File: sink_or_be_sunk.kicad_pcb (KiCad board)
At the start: 2 copper layers, 86.1 x 79.7 mm, 82 parts, among them J1 Grid_Conn_LED, J10 Grid_Conn, J11 Grid_Conn, J12 Grid_Conn, J13 Grid_Conn, J14 Grid_Conn, J15 Grid_Conn, J16 Grid_Conn, J18 Keypad_Conn, J19 Display_Conn, J2 Grid_Conn, J20 JTAG_Conn, J21 Debug_Conn, J22 Battery_Conn, J23 USB_B_Micro, J3 Grid_Conn, J4 Grid_Conn, J5 Grid_Conn, J6 Grid_Conn, J7 Grid_Conn, J8 Grid_Conn, J9 Grid_Conn, M1 Motor_DC, Q1 IRL530, Q2 Q_PMOS_GDS, Q3 2N3704, Q4 2N3704, SW1 SW_DPST, SW2 Reset_SW, U1 SN74HC151N, U2 SwitchingRegulator, U3 MCP73831-2-OT, U4 MCP608, U5 ESP32-WROOM-32, U6 CY7C65213A-28PVXI

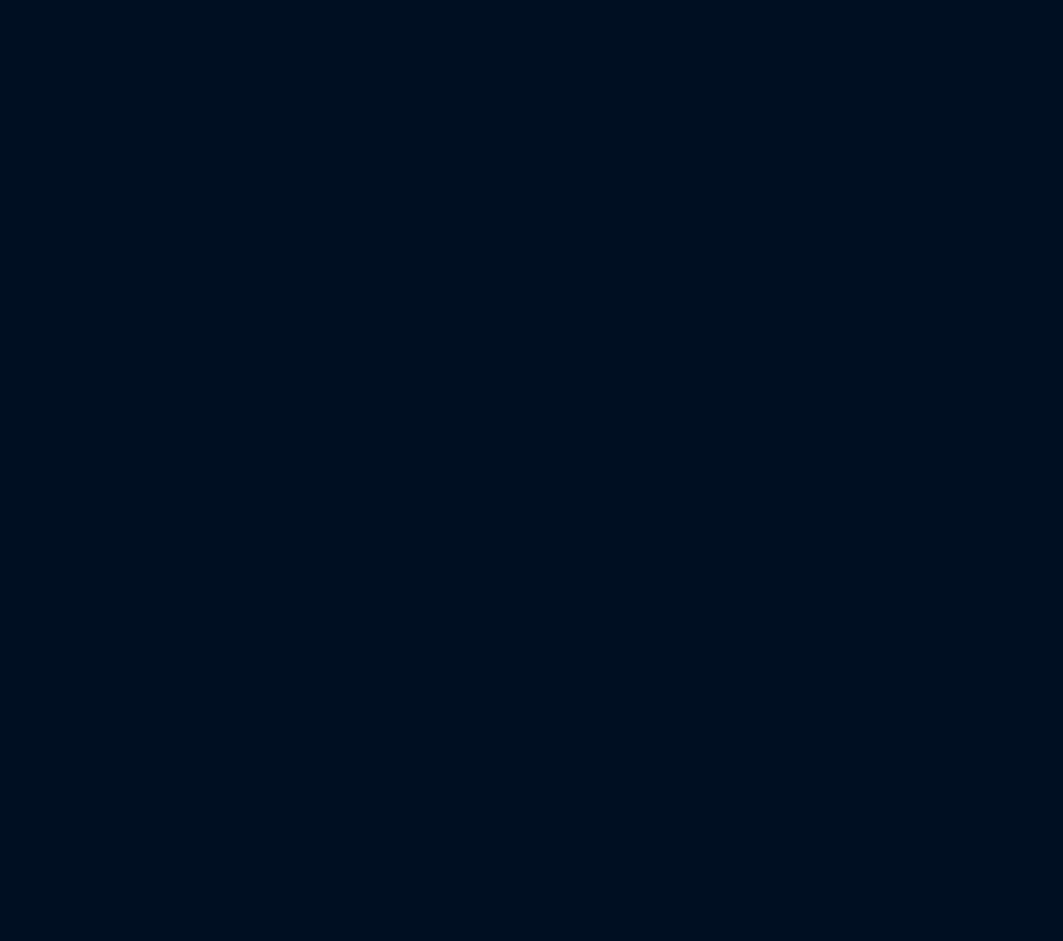
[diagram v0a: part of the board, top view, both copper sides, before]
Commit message: cleaned up footprints
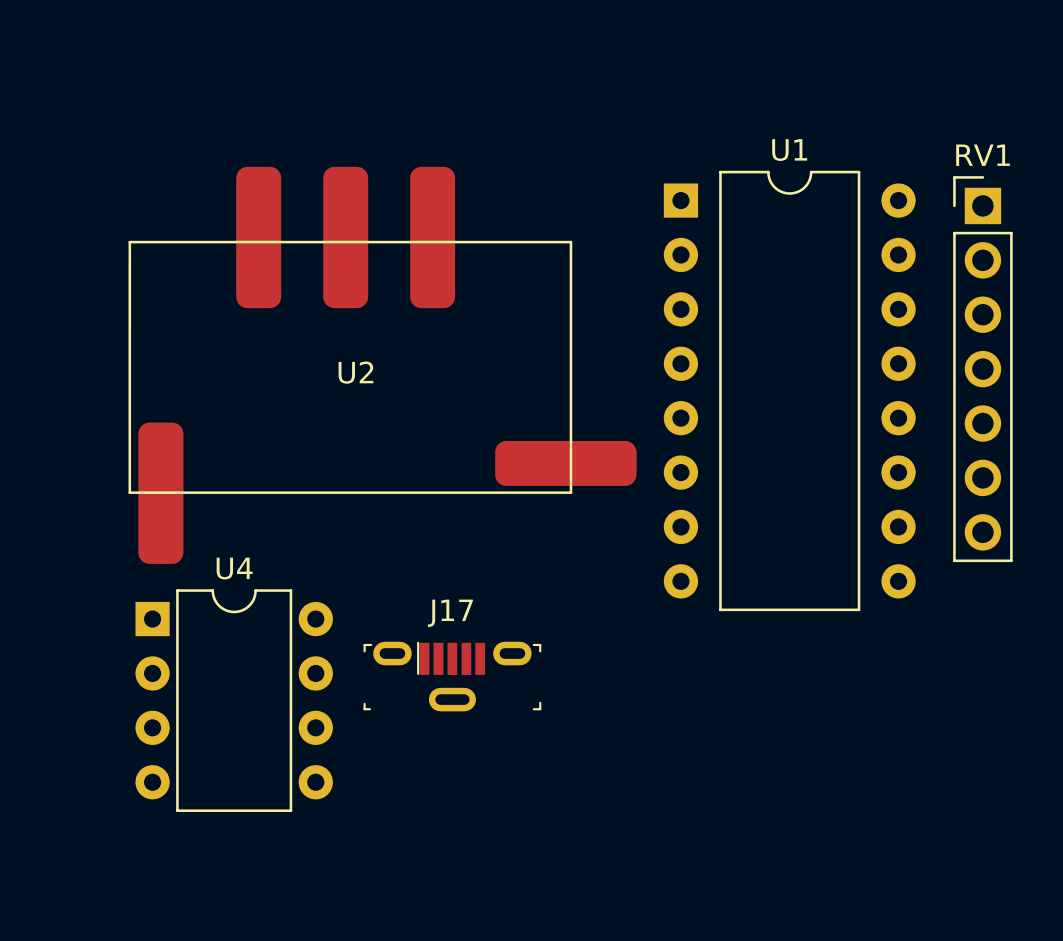
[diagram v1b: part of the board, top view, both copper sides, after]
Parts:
- added J17: USB_B_Micro, PCB_ESP32:USB_Micro_B_Female_Vert_1051330001, F.Cu at (218.7, 112.8)
- added RV1: R_POT, Connector_PinHeader_2.54mm:PinHeader_1x07_P2.54mm_Vertical, F.Cu at (243.5, 91.7)
- added U1: SN74HC151N, Package_DIP:DIP-16_W10.16mm, F.Cu at (229.4, 91.4)
- added U2: SwitchingRegulator, PCB_ESP32:SwitchingRegulator, F.Cu at (214.2, 99.0)
- added U4: MCP608, Package_DIP:DIP-8_W7.62mm, F.Cu at (204.7, 111.0)
- J1: footprint conn:TE_640456-7 -> JST_Conn:TE_640456-7
- J10, J11, J12, J13, J14, J15, J16, J9: footprint conn:TE_640456-2 -> JST_Conn:TE_640456-2
- J2, J3, J4, J5, J6, J7, J8: footprint conn:TE_640456-6 -> JST_Conn:TE_640456-6
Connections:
- U6 pad 15: Net-(J23-Pad3) -> Net-(J17-Pad3)
- U6 pad 16: Net-(J23-Pad2) -> Net-(J17-Pad2)

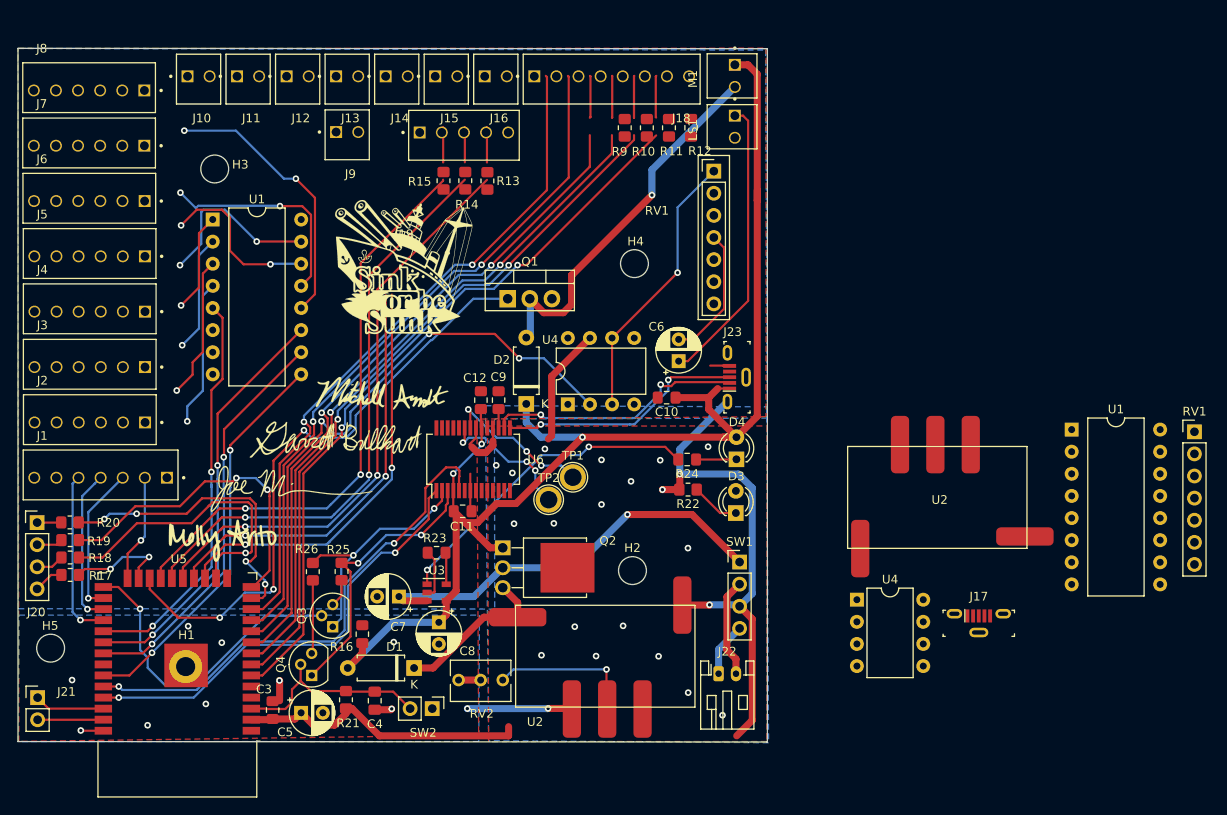
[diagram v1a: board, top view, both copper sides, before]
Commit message: brought over board from regulator
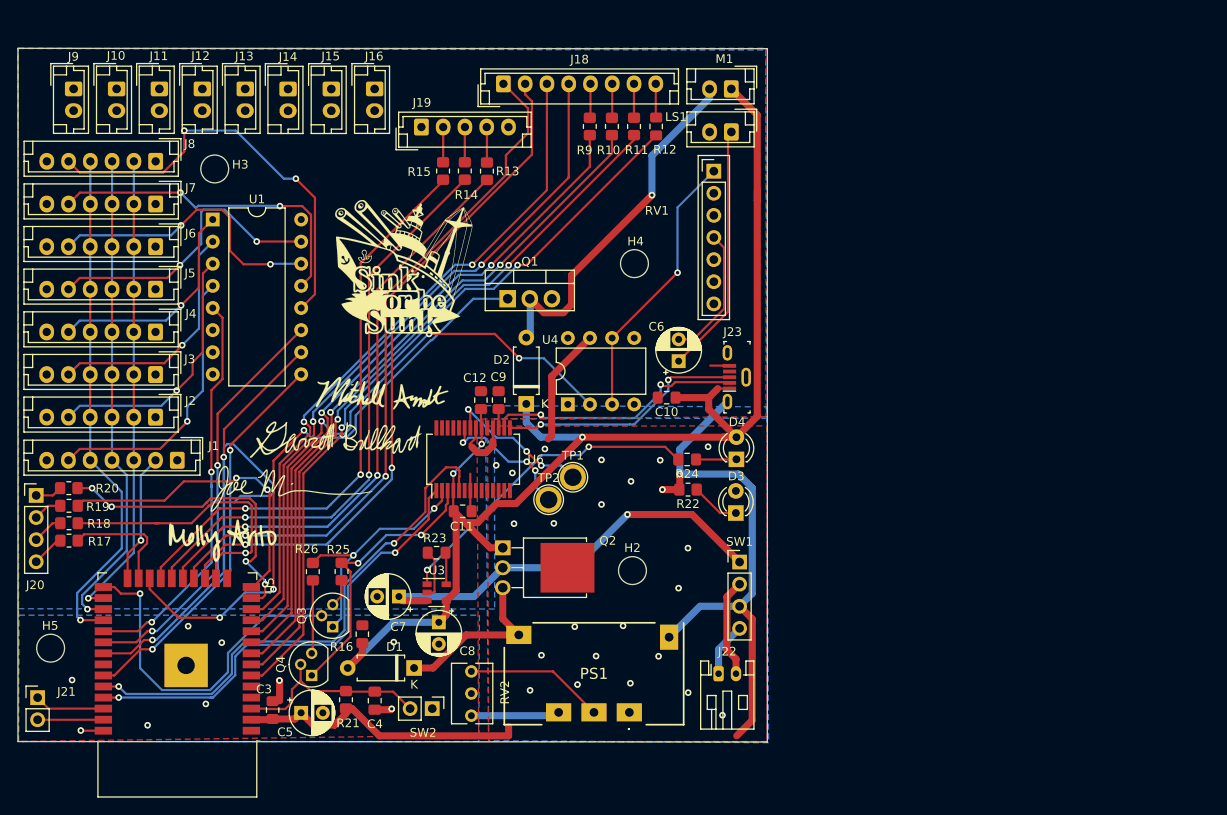
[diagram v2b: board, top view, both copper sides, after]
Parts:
- removed H1: ESP_GND_Pad_Hole, MountingHole:MountingHole_2.2mm_M2_DIN965_Pad
- removed J17: USB_B_Micro, PCB_ESP32:USB_Micro_B_Female_Vert_1051330001
- removed the RV1 at (243.5, 91.7)
- removed the U1 at (229.4, 91.4)
- removed U2 (x2): SwitchingRegulator, PCB_ESP32:SwitchingRegulator
- removed the U4 at (204.7, 111.0)
- added PS1: DNT04S0A0S03NFA, PCB_ESP32:DNT04S0A0S03NFA, F.Cu at (174.5, 119.5)
- J1: footprint JST_Conn:TE_640456-7 -> Connector_JST:JST_EH_B7B-EH-A_1x07_P2.50mm_Vertical
- J10, J11, J12, J13, J14, J15, J16, J9: footprint JST_Conn:TE_640456-2 -> Connector_JST:JST_EH_B2B-EH-A_1x02_P2.50mm_Vertical
- J18: footprint conn:TE_640456-8 -> Connector_JST:JST_EH_B8B-EH-A_1x08_P2.50mm_Vertical
- J19: footprint conn:TE_640456-5 -> Connector_JST:JST_EH_B5B-EH-A_1x05_P2.50mm_Vertical
- J2, J3, J4, J5, J6, J7, J8: footprint JST_Conn:TE_640456-6 -> Connector_JST:JST_EH_B6B-EH-A_1x06_P2.50mm_Vertical
- LS1, M1: footprint conn:TE_640456-2 -> Connector_JST:JST_EH_B2B-EH-A_1x02_P2.50mm_Vertical
- U5: footprint RF_Module:ESP32-WROOM-32 -> PCB_ESP32:ESP32-WROOM-32
- moved J9 30.6 mm to (114.8, 52.3), turned to 270 degrees
- moved J16 12.7 mm to (149.3, 52.3), turned to 270 degrees
- moved J15 12.0 mm to (144.4, 52.3), turned to 270 degrees
- moved J14 11.3 mm to (139.4, 52.3), turned to 270 degrees
- moved J13 10.5 mm to (134.5, 52.3), turned to 270 degrees
- moved J12 9.78 mm to (129.5, 52.3), turned to 270 degrees
- moved J11 9.04 mm to (124.6, 52.3), turned to 270 degrees
- moved J10 8.27 mm to (119.7, 52.3), turned to 270 degrees
- moved J8 8.24 mm to (124.2, 60.6), turned to 180 degrees
- moved J7 6.82 mm to (124.2, 65.5), turned to 180 degrees
- moved J6 5.39 mm to (124.2, 70.4), turned to 180 degrees
- moved R10 4.02 mm to (176.6, 56.6)
- moved R9 4.02 mm to (174.0, 56.6)
- moved R11 4.02 mm to (179.1, 56.6)
- moved R12 4.02 mm to (181.7, 56.6)
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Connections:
- U6 pad 15: Net-(J17-Pad3) -> Net-(J23-Pad3)
- U6 pad 16: Net-(J17-Pad2) -> Net-(J23-Pad2)
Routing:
- net /MUX_COL_SEL0: track 19.6 -> 59.1 mm
- net /MUX_COL_SEL2: track 18.1 -> 56.4 mm
- net /MUX_COL_SEL1: track 17.2 -> 54.1 mm
- net /KEYPAD_COL0: track 48.6 -> 80.8 mm
- net /KEYPAD_COL1: track 48.8 -> 80.0 mm
- net /MUX_ROW_SEL1: track 47.3 -> 75.3 mm
- net /MUX_R7: track 31.5 -> 48.7 mm
- net /MUX_R0: track 16.8 -> 32.3 mm
- net /MUX_R2: track 13.3 -> 27.8 mm
- net /MUX_R3: track 11.4 -> 25.6 mm
- net /MUX_R4: track 20.2 -> 34.2 mm
- net /MUX_R5: track 19.5 -> 33.4 mm
- net /MUX_R1: track 16.7 -> 30.4 mm
- net /MUX_R6: track 24.9 -> 38.3 mm
- net Net-(C6-Pad1): track 33.3 -> 28.8 mm
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
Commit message: merged connectors and regulator footprint
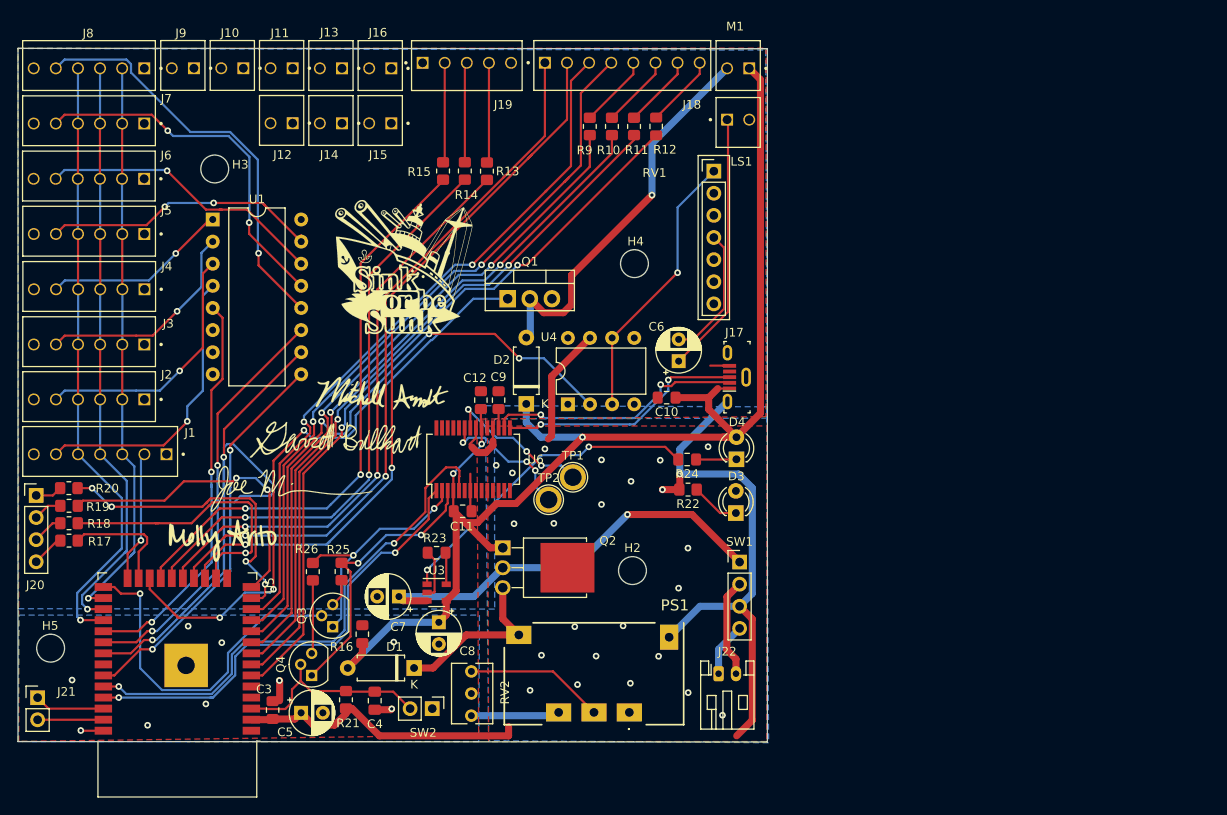
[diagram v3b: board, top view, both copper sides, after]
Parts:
- removed J23: USB_B_Micro, PCB_ESP32:USB_Micro_B_Female_Vert_1051330001
- added J17: USB_B_Micro, PCB_ESP32:USB_Micro_B_Female_Vert_1051330001, F.Cu at (190.1, 85.4)
- J1: value Grid_Conn_LED -> Grid_Conn; footprint Connector_JST:JST_EH_B7B-EH-A_1x07_P2.50mm_Vertical -> JST_Conn:TE_640456-7
- J10, J11, J12, J13, J14, J15, J16, J9: value Grid_Conn -> 640456-2; footprint Connector_JST:JST_EH_B2B-EH-A_1x02_P2.50mm_Vertical -> JST_Conn:TE_640456-2
- J18: footprint Connector_JST:JST_EH_B8B-EH-A_1x08_P2.50mm_Vertical -> JST_Conn:TE_640456-8
- J19: footprint Connector_JST:JST_EH_B5B-EH-A_1x05_P2.50mm_Vertical -> JST_Conn:TE_640456-5
- J2, J3, J4, J5, J6, J7, J8: value Grid_Conn -> 640456-6; footprint Connector_JST:JST_EH_B6B-EH-A_1x06_P2.50mm_Vertical -> JST_Conn:TE_640456-6
- LS1, M1: footprint Connector_JST:JST_EH_B2B-EH-A_1x02_P2.50mm_Vertical -> JST_Conn:TE_640456-2
- moved J11 15.5 mm to (139.9, 49.9), turned to 0 degrees
- moved J10 14.7 mm to (134.3, 49.9), turned to 0 degrees
- moved J9 14.0 mm to (128.6, 49.9), turned to 0 degrees
- moved J13 11.4 mm to (145.6, 49.9), turned to 0 degrees
- moved J12 11.1 mm to (139.9, 56.2), turned to 0 degrees
- moved J8 10.8 mm to (122.9, 49.9), turned to 0 degrees
- moved J7 9.34 mm to (122.9, 56.3), turned to 0 degrees
- moved J6 7.90 mm to (122.9, 62.6), turned to 0 degrees
- moved J19 7.38 mm to (154.8, 49.3), turned to 180 degrees
- moved J14 7.34 mm to (145.6, 56.2), turned to 0 degrees
- moved J15 7.29 mm to (151.2, 49.9), turned to 0 degrees
- moved J5 6.47 mm to (122.9, 69.0), turned to 0 degrees
- moved J18 5.35 mm to (168.9, 49.3), turned to 180 degrees
- moved J4 5.06 mm to (122.9, 75.3), turned to 0 degrees
- moved J16 4.39 mm to (151.2, 56.2), turned to 0 degrees
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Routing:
- net /MUX_COL_SEL1: track 54.1 -> 65.8 mm
- net /MUX_COL_SEL2: track 56.4 -> 67.9 mm
- net /MUX_COL_SEL0: track 59.1 -> 70.7 mm
- net Net-(J19-Pad3): track 4.05 -> 11.5 mm
- net Net-(J19-Pad2): track 4.05 -> 11.5 mm
- net Net-(J19-Pad4): track 4.08 -> 11.5 mm
- net /KEYPAD_COL3: track 79.4 -> 84.6 mm
- net /KEYPAD_COL2: track 77.0 -> 81.6 mm
- net Net-(J18-Pad5): track 3.93 -> 8.50 mm
- net Net-(J18-Pad8): track 3.89 -> 8.43 mm
- net Net-(J18-Pad6): track 3.91 -> 8.44 mm
- net Net-(J18-Pad7): track 3.90 -> 8.40 mm
- net /KEYPAD_COL1: track 80.0 -> 84.4 mm
- net /MUX_R3: track 25.6 -> 21.3 mm
- net /MUX_R6: track 38.3 -> 42.0 mm
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
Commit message: updated dimensions
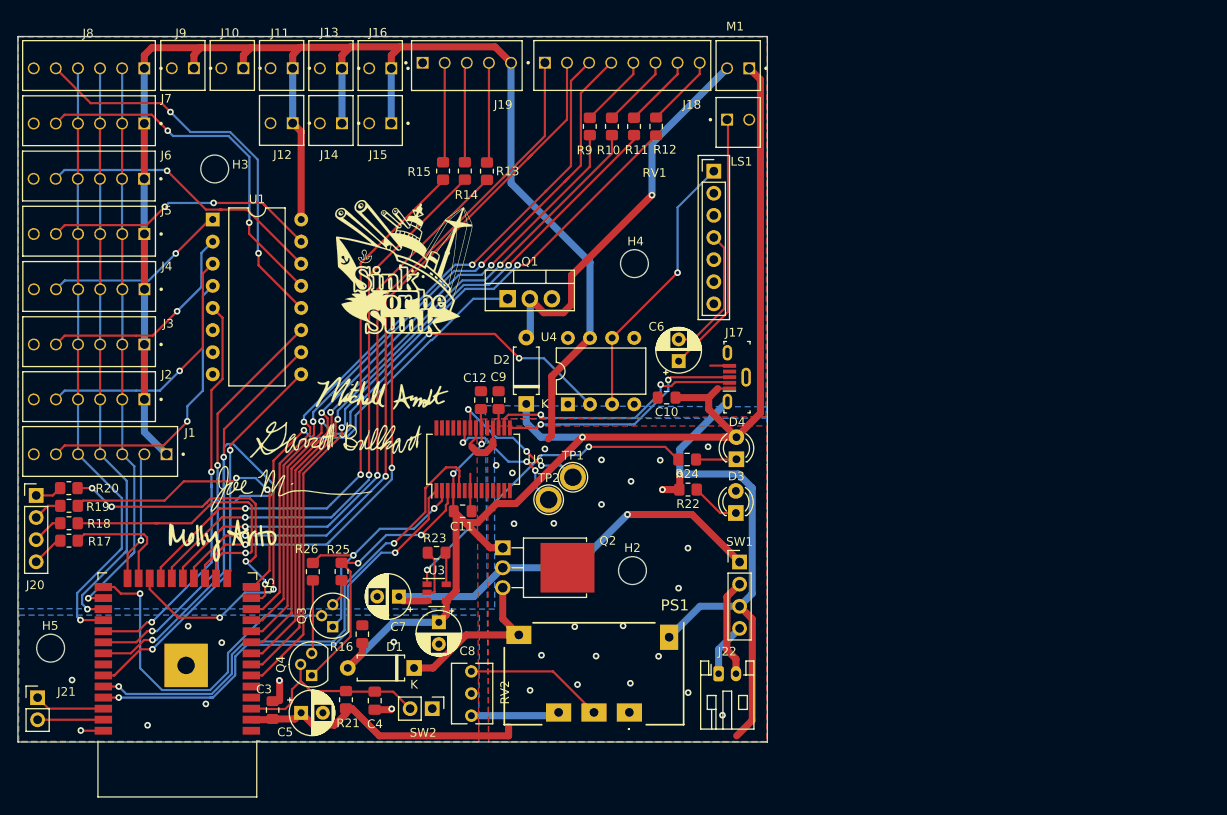
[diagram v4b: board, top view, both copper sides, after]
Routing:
- net +3V3: track 47.5 -> 217.1 mm
- net /MUX_R7: track 48.4 -> 47.0 mm, vias 1 -> 2
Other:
- board size 86.1 x 79.7 mm -> 86.1 x 81 mm

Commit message: fixed issue with attack connector labels
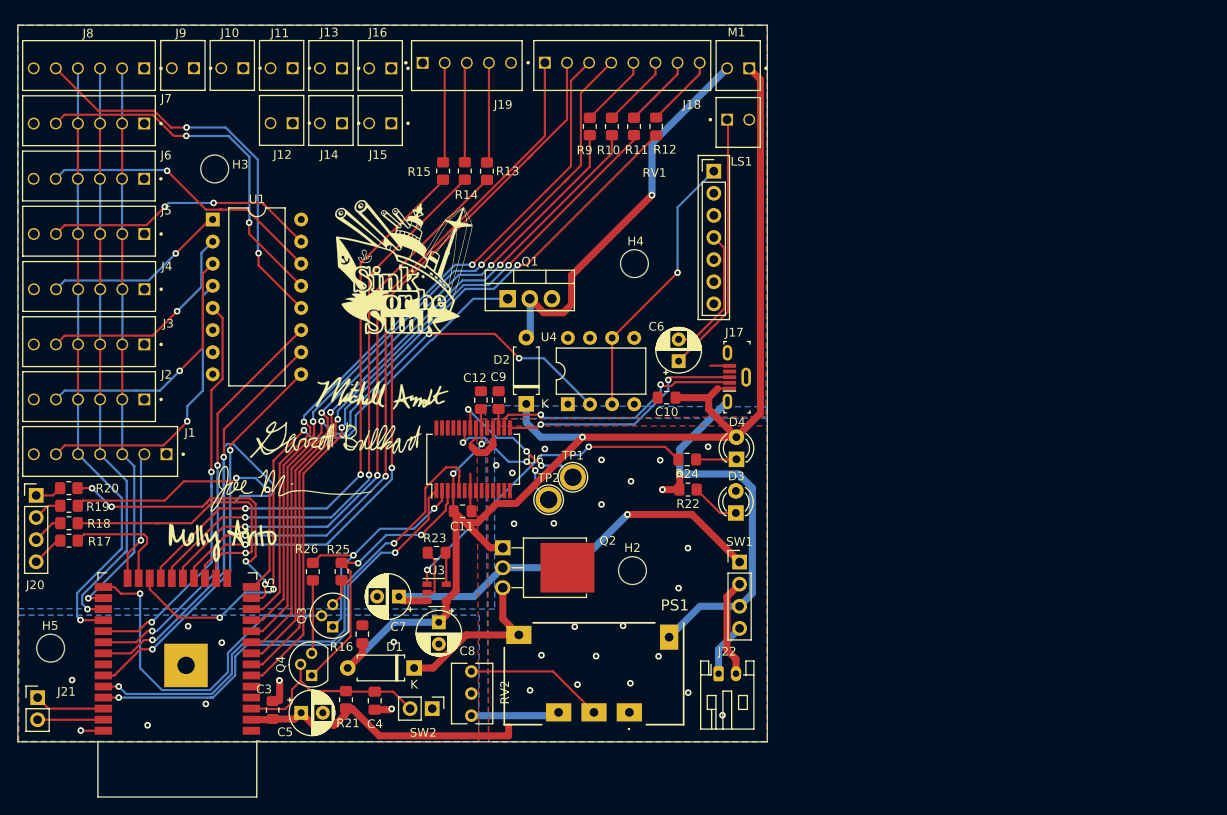
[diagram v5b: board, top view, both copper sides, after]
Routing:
- net +3V3: track 217.1 -> 34.0 mm
- net GND: track 94.5 -> 78.3 mm
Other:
- board size 86.1 x 81 mm -> 86.1 x 82.3 mm
